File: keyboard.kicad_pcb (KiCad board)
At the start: 2 copper layers, 359.9 x 94.6 mm, 211 parts, among them IC1 ATMEGA32U4, J1 USB C, X1 ASX3F

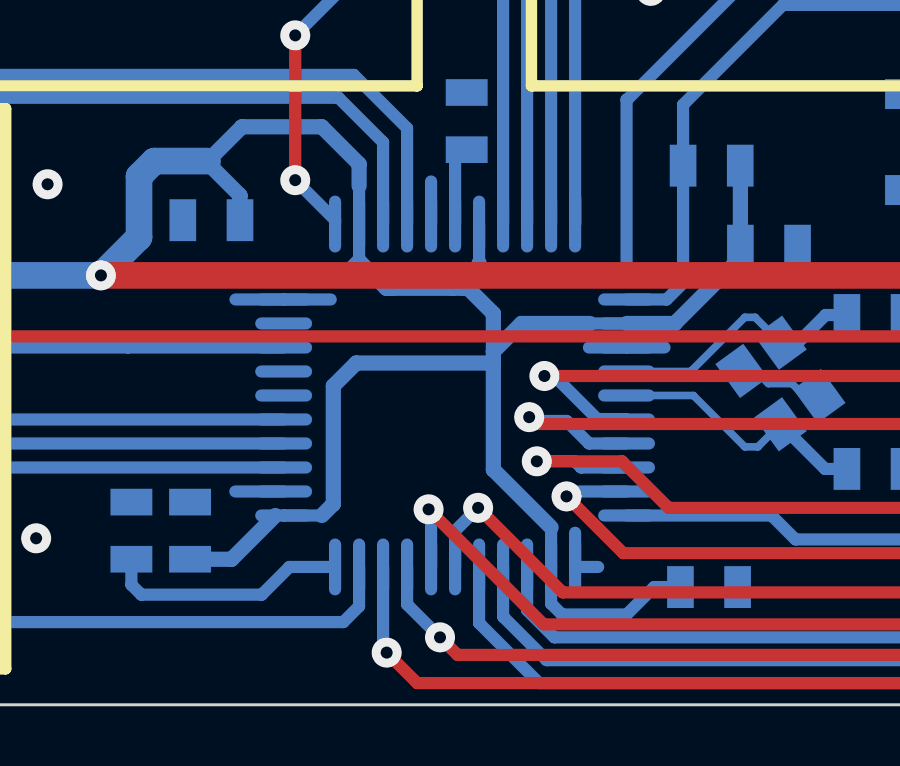
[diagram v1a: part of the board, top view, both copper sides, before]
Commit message: Change footprint for MCU
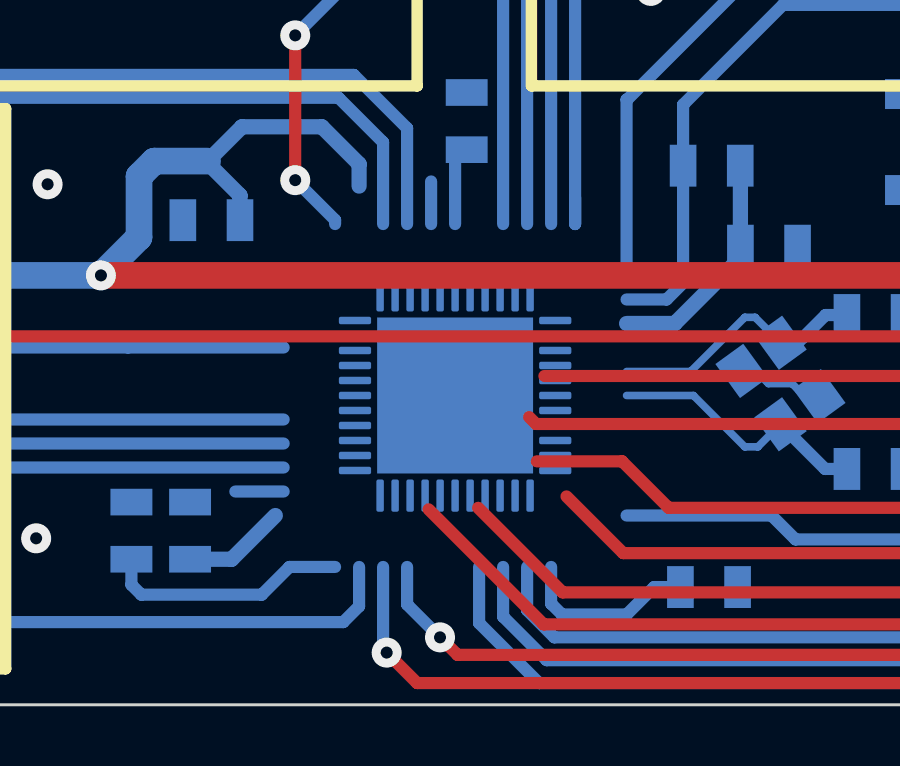
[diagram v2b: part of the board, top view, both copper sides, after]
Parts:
- IC1: footprint tqfp:TQFP44 -> Package_DFN_QFN:QFN-44-1EP_7x7mm_P0.5mm_EP5.2x5.2mm
- S64: footprint mx1a:MX1A_no3d -> mx1a:MX1A
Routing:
- net VCC: track 909.1 -> 870.9 mm
- net GND: track 13.6 -> 5.97 mm
- net /col16: track 343.1 -> 338.1 mm, vias 4 -> 3
- net /col15: track 306.0 -> 302.5 mm, vias 4 -> 3
- net /col17: track 380.8 -> 377.4 mm, vias 2 -> 1
- net /col11: track 227.2 -> 224.9 mm, vias 2 -> 1
- net /col12: track 251.5 -> 249.5 mm, vias 2 -> 1
- net /col10: track 199.8 -> 197.9 mm, vias 2 -> 1

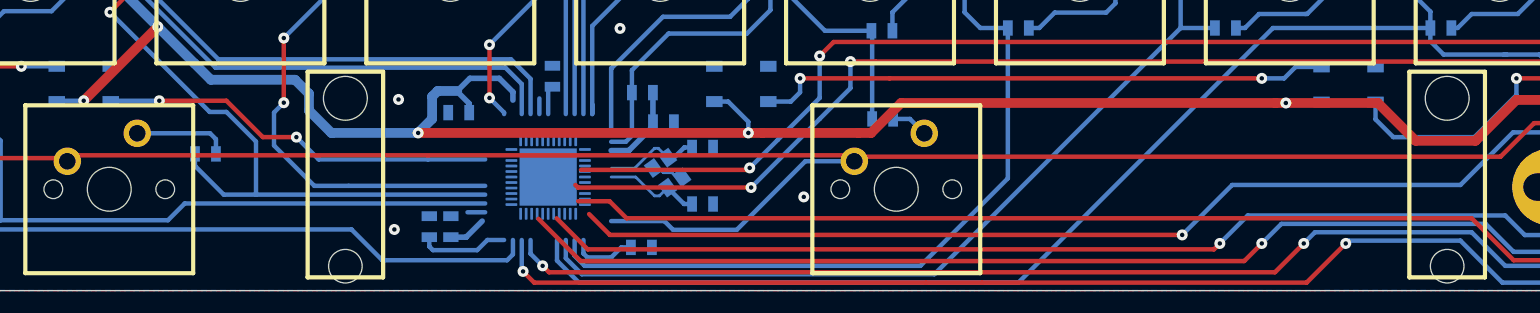
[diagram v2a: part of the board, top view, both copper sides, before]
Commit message: Connect a few tracks to new QFN-44 package
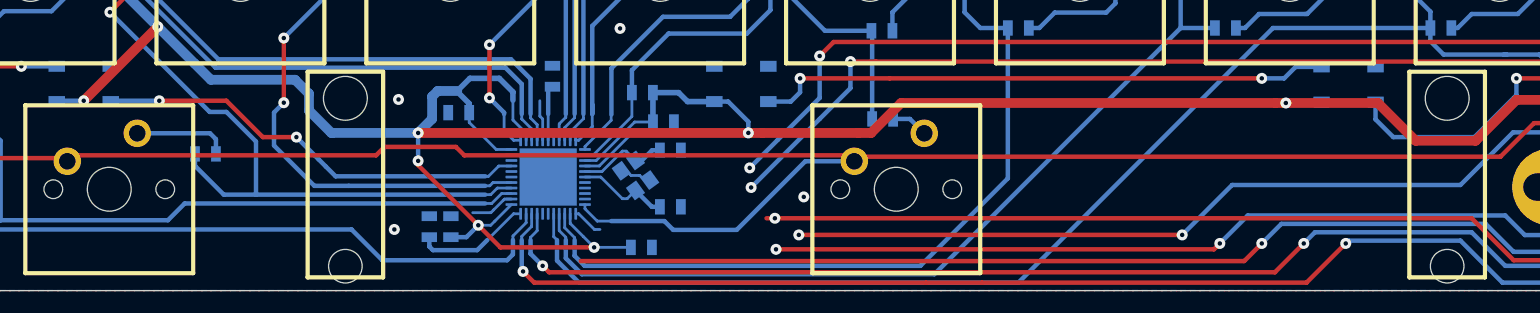
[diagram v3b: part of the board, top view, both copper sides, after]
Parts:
- moved X1 2.93 mm to (169.2, 148.8)
- moved C1 2.93 mm to (172.4, 146.5)
- moved C2 2.93 mm to (172.4, 151.6)
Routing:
- net VCC: track 870.9 -> 916.1 mm, vias 18 -> 21
- net /col11: track 224.9 -> 203.8 mm, vias 1 -> 2
- net /col10: track 197.9 -> 178.1 mm, vias 1 -> 2
- net /col17: track 377.4 -> 359.7 mm, vias 1 -> 2
- net /col15: track 302.5 -> 286.4 mm
- net /col16: track 338.1 -> 322.9 mm
- net GND: track 5.97 -> 18.6 mm
- net /col12: track 249.5 -> 244.0 mm
- net /row5: track 373.3 -> 377.2 mm
- net /row4: track 374.6 -> 378.2 mm
- net /leds: track 36.2 -> 39.6 mm
- net /col5: track 83.0 -> 86.4 mm
- net /col1: track 165.7 -> 168.6 mm
- net /row3: track 415.5 -> 418.4 mm
- net /col7: track 131.8 -> 134.6 mm
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
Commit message: Connect new MCU and reduce trace width
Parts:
- moved C3 1.56 mm to (160.1, 140.1)
- moved C2 1.12 mm to (172.3, 150.5), turned to 35 degrees
- moved C6 0.41 mm to (169.8, 155.7)
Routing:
- net /col11: track 203.8 -> 227.4 mm
- net /col10: track 178.1 -> 199.0 mm
- net /col17: track 359.7 -> 377.6 mm
- net /col16: track 322.9 -> 340.6 mm, vias 3 -> 2
- net /col15: track 286.4 -> 303.5 mm, vias 3 -> 2
- net /col12: track 244.0 -> 254.2 mm, vias 1 -> 2
- net VCC: track 916.1 -> 922.2 mm, vias 21 -> 22
- net /col14: track 313.5 -> 317.8 mm
- net /col13: track 280.1 -> 284.3 mm
- net GND: track 18.6 -> 22.5 mm, vias 12 -> 13
- net /col5: track 86.4 -> 87.5 mm
- net Net-(IC1-Pad4): track 126.6 -> 125.6 mm
- net Net-(IC1-Pad3): track 127.1 -> 126.1 mm
- net /col1: track 168.6 -> 167.7 mm

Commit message: Connect diode pads
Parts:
- D1, D10, D11, D12, D13, D14, D15, D16, D17, D18, D19, D2, D21, D22, D23, D24, D26, D27, D28, D29, D3, D30, D31, D32, D33, D34, D36, D37, D38, D39, D4, D41, D42, D43, D44, D46, D47, D48, D49, D5, D51, D52, D53, D54, D55, D56, D57, D58, D59, D6, D60, D61, D62, D64, D65, D66, D67, D68, D69, D7, D70, D71, D72, D73, D74, D75, D76, D77, D78, D79, D8, D80, D81, D82, D83, D84, D85, D86, D87, D88, D89: footprint 0805:0805D -> Diode_SMD:D_SOD-323F
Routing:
- net VCC: track 922.2 -> 918.3 mm
- net Net-(D57-Pad2): track 15.8 -> 13.0 mm
- net /col3: track 124.0 -> 126.7 mm
- net /col1: track 167.7 -> 170.2 mm
- net /col12: track 254.2 -> 256.6 mm
- net /col2: track 147.4 -> 149.6 mm
- net /col9: track 180.0 -> 181.4 mm
- net /col6: track 120.1 -> 121.5 mm
- net /col5: track 87.5 -> 88.7 mm
- net Net-(D56-Pad2): track 10.7 -> 11.8 mm
- net Net-(D46-Pad2): track 10.9 -> 12.0 mm
- net Net-(D49-Pad2): track 15.6 -> 16.7 mm
- net /col7: track 134.8 -> 135.7 mm
- net Net-(D41-Pad2): track 10.8 -> 11.7 mm
- net Net-(D31-Pad2): track 10.3 -> 11.2 mm
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
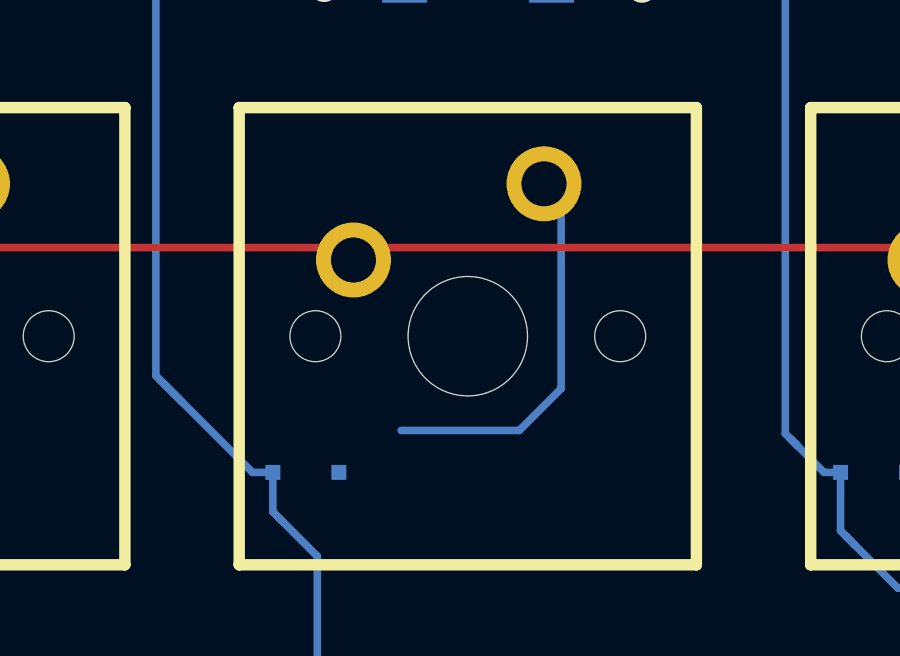
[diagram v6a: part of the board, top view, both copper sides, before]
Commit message: Fix cable not connected
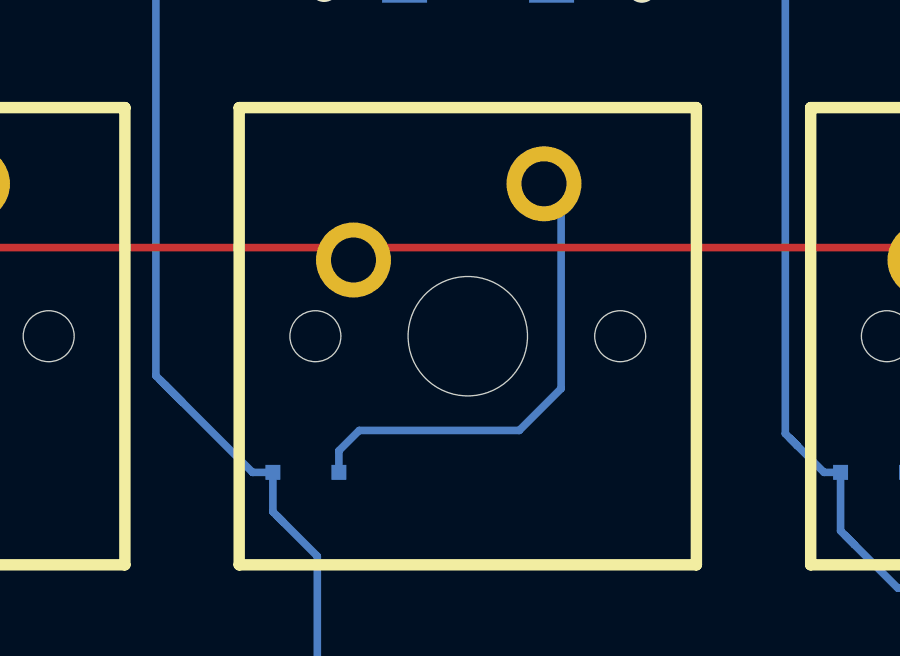
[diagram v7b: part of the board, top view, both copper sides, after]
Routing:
- net Net-(D57-Pad2): track 13.0 -> 16.0 mm
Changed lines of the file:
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@@
     (thickness 1.6002)
     (drawings 87)
-    (tracks 1867)
+    (tracks 1869)
     (zones 0)
     (modules 211)
@@
   )
   (setup
-    (last_trace_width 0.4064)
+    (last_trace_width 0.254)
     (user_trace_width 0.254)
     (trace_clearance 0.2032)
@@
       (effects (font (size 1 1) (thickness 0.15)) (justify mirror))
     )
-    (pad "" smd roundrect (at 1.95 -1.95 270) (size 1.05 1.05) (layers B.Paste) (roundrect_rratio 0.238095))
-    (pad "" smd roundrect (at 1.95 -0.65 270) (size 1.05 1.05) (layers B.Paste) (roundrect_rratio 0.238095))
-    (pad "" smd roundrect (at 1.95 0.65 270) (size 1.05 1.05) (layers B.Paste) (roundrect_rratio 0.238095))
-    (pad "" smd roundrect (at 1.95 1.95 270) (size 1.05 1.05) (layers B.Paste) (roundrect_rratio 0.238095))
-    (pad "" smd roundrect (at 0.65 -1.95 270) (size 1.05 1.05) (layers B.Paste) (roundrect_rratio 0.238095))
-    (pad "" smd roundrect (at 0.65 -0.65 270) (size 1.05 1.05) (layers B.Paste) (roundrect_rratio 0.238095))
-    (pad "" smd roundrect (at 0.65 0.65 270) (size 1.05 1.05) (layers B.Paste) (roundrect_rratio 0.238095))
-    (pad "" smd roundrect (at 0.65 1.95 270) (size 1.05 1.05) (layers B.Paste) (roundrect_rratio 0.238095))
-    (pad "" smd roundrect (at -0.65 -1.95 270) (size 1.05 1.05) (layers B.Paste) (roundrect_rratio 0.238095))
-    (pad "" smd roundrect (at -0.65 -0.65 270) (size 1.05 1.05) (layers B.Paste) (roundrect_rratio 0.238095))
-    (pad "" smd roundrect (at -0.65 0.65 270) (size 1.05 1.05) (layers B.Paste) (roundrect_rratio 0.238095))
-    (pad "" smd roundrect (at -0.65 1.95 270) (size 1.05 1.05) (layers B.Paste) (roundrect_rratio 0.238095))
-    (pad "" smd roundrect (at -1.95 -1.95 270) (size 1.05 1.05) (layers B.Paste) (roundrect_rratio 0.238095))
-    (pad "" smd roundrect (at -1.95 -0.65 270) (size 1.05 1.05) (layers B.Paste) (roundrect_rratio 0.238095))
-    (pad "" smd roundrect (at -1.95 0.65 270) (size 1.05 1.05) (layers B.Paste) (roundrect_rratio 0.238095))
-    (pad "" smd roundrect (at -1.95 1.95 270) (size 1.05 1.05) (layers B.Paste) (roundrect_rratio 0.238095))
+    (pad "" smd roundrect (at 1.95 -1.95 270) (size 1.05 1.05) (layers B.Paste) (roundrect_rratio 0.2380942857142857))
+    (pad "" smd roundrect (at 1.95 -0.65 270) (size 1.05 1.05) (layers B.Paste) (roundrect_rratio 0.2380942857142857))
+    (pad "" smd roundrect (at 1.95 0.65 270) (size 1.05 1.05) (layers B.Paste) (roundrect_rratio 0.2380942857142857))
+    (pad "" smd roundrect (at 1.95 1.95 270) (size 1.05 1.05) (layers B.Paste) (roundrect_rratio 0.2380942857142857))
+    (pad "" smd roundrect (at 0.65 -1.95 270) (size 1.05 1.05) (layers B.Paste) (roundrect_rratio 0.2380942857142857))
+    (pad "" smd roundrect (at 0.65 -0.65 270) (size 1.05 1.05) (layers B.Paste) (roundrect_rratio 0.2380942857142857))
+    (pad "" smd roundrect (at 0.65 0.65 270) (size 1.05 1.05) (layers B.Paste) (roundrect_rratio 0.2380942857142857))
+    (pad "" smd roundrect (at 0.65 1.95 270) (size 1.05 1.05) (layers B.Paste) (roundrect_rratio 0.2380942857142857))
+    (pad "" smd roundrect (at -0.65 -1.95 270) (size 1.05 1.05) (layers B.Paste) (roundrect_rratio 0.2380942857142857))
+    (pad "" smd roundrect (at -0.65 -0.65 270) (size 1.05 1.05) (layers B.Paste) (roundrect_rratio 0.2380942857142857))
+    (pad "" smd roundrect (at -0.65 0.65 270) (size 1.05 1.05) (layers B.Paste) (roundrect_rratio 0.2380942857142857))
+    (pad "" smd roundrect (at -0.65 1.95 270) (size 1.05 1.05) (layers B.Paste) (roundrect_rratio 0.2380942857142857))
+    (pad "" smd roundrect (at -1.95 -1.95 270) (size 1.05 1.05) (layers B.Paste) (roundrect_rratio 0.2380942857142857))
+    (pad "" smd roundrect (at -1.95 -0.65 270) (size 1.05 1.05) (layers B.Paste) (roundrect_rratio 0.2380942857142857))
+    (pad "" smd roundrect (at -1.95 0.65 270) (size 1.05 1.05) (layers B.Paste) (roundrect_rratio 0.2380942857142857))
+    (pad "" smd roundrect (at -1.95 1.95 270) (size 1.05 1.05) (layers B.Paste) (roundrect_rratio 0.2380942857142857))
     (pad 45 smd rect (at 0 0 270) (size 5.2 5.2) (layers B.Cu B.Mask))
     (pad 44 smd roundrect (at -2.5 3.3375 270) (size 0.25 1.075) (layers B.Cu B.Paste B.Mask) (roundrect_rratio 0.25)
@@
   (segment (start 284.1752 74.8792) (end 284.1752 69.38772) (width 0.254) (layer B.Cu) (net 57))
   (segment (start 284.1752 75.2602) (end 284.1752 74.8792) (width 0.254) (layer B.Cu) (net 57))
-  (segment (start 288.29 96.012) (end 292.227 96.012) (width 0.254) (layer B.Cu) (net 58))
-  (segment (start 292.227 96.012) (end 293.624 94.615) (width 0.254) (layer B.Cu) (net 58))
-  (segment (start 293.624 94.615) (end 293.624 88.36152) (width 0.254) (layer B.Cu) (net 58))
-  (segment (start 293.624 88.36152) (end 293.0525 87.79002) (width 0.254) (layer B.Cu) (net 58))
+  (segment (start 286.215 96.69) (end 286.215 97.409) (width 0.254) (layer B.Cu) (net 58))
+  (segment (start 286.893 96.012) (end 286.215 96.69) (width 0.254) (layer B.Cu) (net 58))
+  (segment (start 292.227 96.012) (end 286.893 96.012) (width 0.254) (layer B.Cu) (net 58))
+  (segment (start 293.624 94.615) (end 292.227 96.012) (width 0.254) (layer B.Cu) (net 58))
+  (segment (start 293.624 88.36152) (end 293.624 94.615) (width 0.254) (layer B.Cu) (net 58))
+  (segment (start 293.0525 87.79002) (end 293.624 88.36152) (width 0.254) (layer B.Cu) (net 58))
   (segment (start 297.815 106.84002) (end 297.815 106.84002) (width 0.254) (layer B.Cu) (net 59))
   (segment (start 297.815 106.84002) (end 298.09694 107.20832) (width 0.254) (layer B.Cu) (net 59))
